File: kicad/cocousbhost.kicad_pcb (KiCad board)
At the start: 2 copper layers, 98.3 x 87.3 mm, 31 parts, among them J1 Conn_01x03_Male, J2 Jumper_2_Bridged, J3 USB_A, Q1 2N2222, SW1 SW_DIP_x07, U1 74LS30, U2 Coco_Cart_Connector, U3 74LS682, U4 74LS04, U5 74LS74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

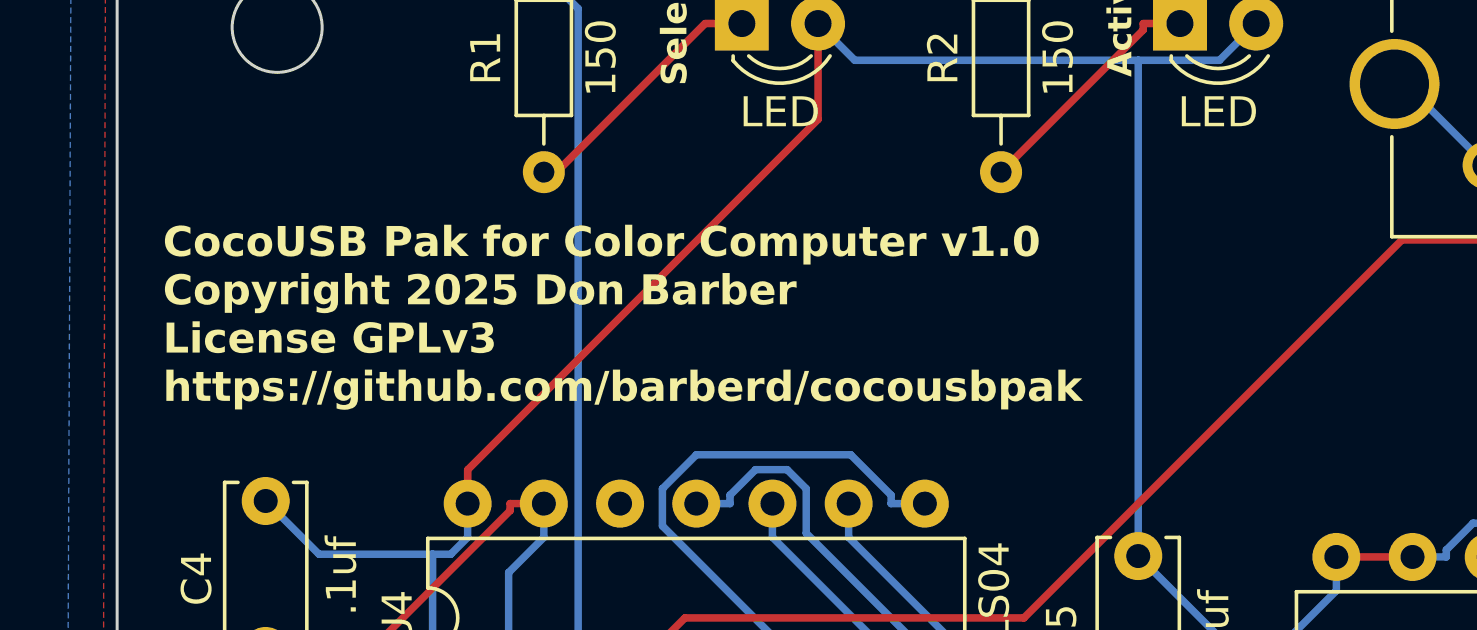
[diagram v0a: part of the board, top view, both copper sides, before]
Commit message: Renamed to CoCo USB Host
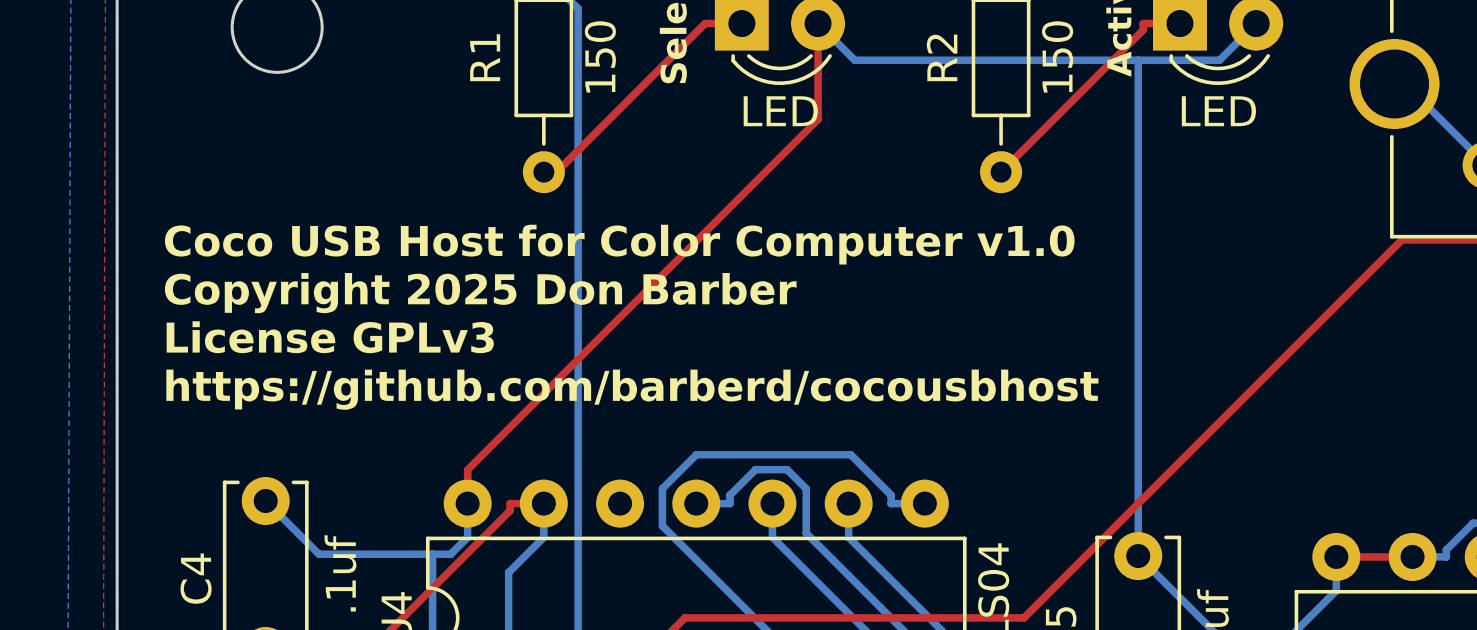
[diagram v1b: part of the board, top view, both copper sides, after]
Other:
- board text added: "Coco USB Host for Color Computer v1.0 Copyright 2025 Don Barber License GPLv3 https://github.com/barberd/cocousbhost"
- board text removed: "CocoUSB Pak for Color Computer v1.0 Copyright 2025 Don Barber License GPLv3 https://github.com/barberd/cocousbpak"
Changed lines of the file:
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@@
 		)
 	)
-	(gr_text "CocoUSB Pak for Color Computer v1.0\nCopyright 2025 Don Barber\nLicense GPLv3\nhttps://github.com/barberd/cocousbpak"
+	(gr_text "Coco USB Host for Color Computer v1.0\nCopyright 2025 Don Barber\nLicense GPLv3\nhttps://github.com/barberd/cocousbhost"
 		(at 67.945 47.625 0)
 		(layer "F.SilkS")
